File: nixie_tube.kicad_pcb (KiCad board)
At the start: 2 copper layers, 25.8 x 56.3 mm, 32 parts, among them J1 Conn_01x06_Male, J11 dc003a, J2 Conn_01x06_Female, J3 Conn_01x01_Male, J4 Conn_01x01_Female, Q1 SS8550, Q2 FQD5N60C, Q3 MMBTA42LT1, Q4 AO3407, U1 MC34063

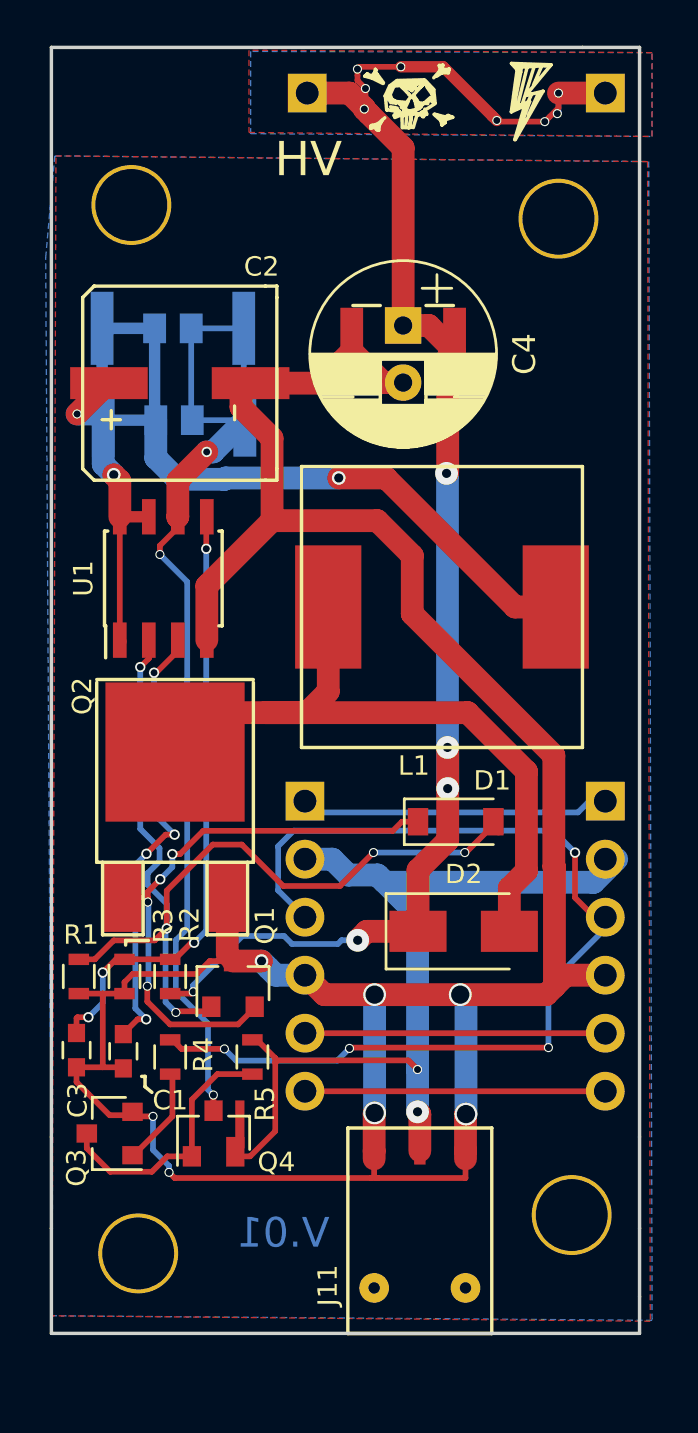
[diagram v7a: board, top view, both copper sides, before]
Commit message: added via stiching around the board
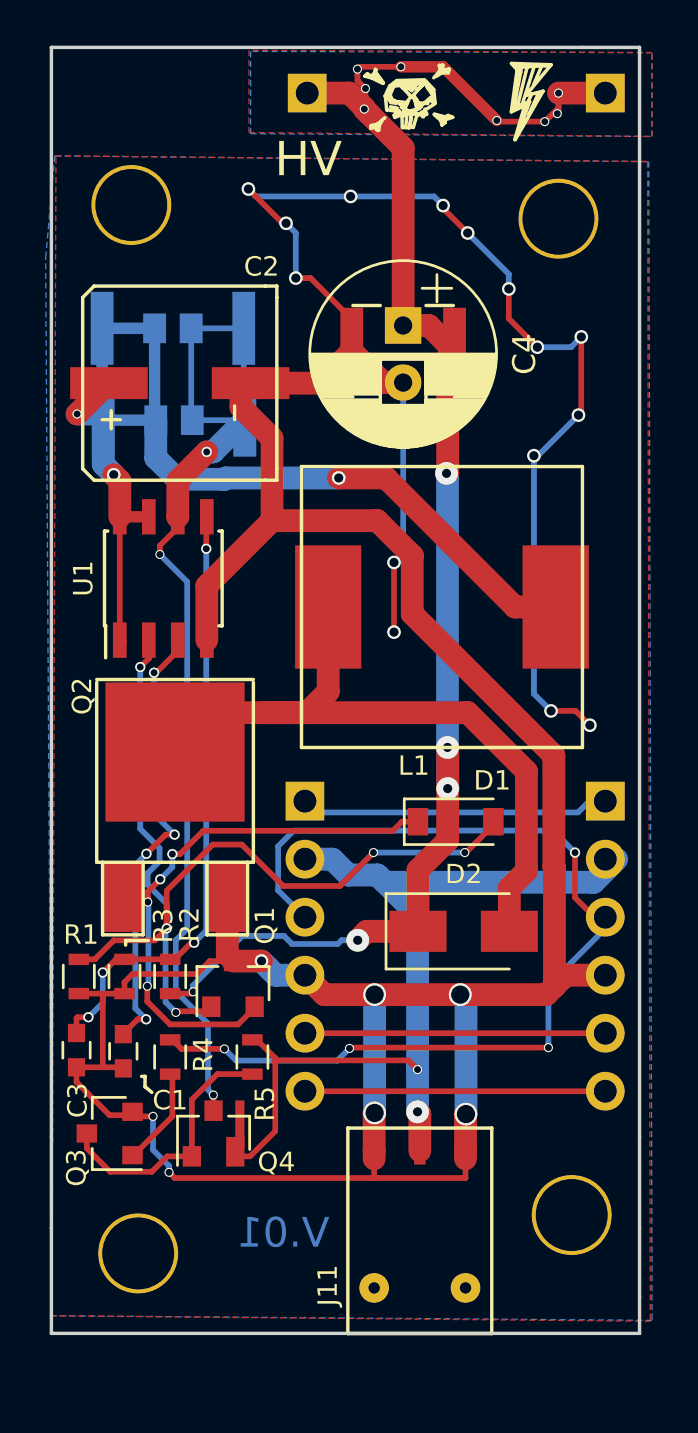
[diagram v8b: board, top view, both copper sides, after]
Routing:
- net GND: track 119.4 -> 178.4 mm, vias 7 -> 22
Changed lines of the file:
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@@
     (links 56)
     (no_connects 0)
-    (area 166.424999 79.724999 192.325001 136.175001)
+    (area 156.600001 76.825 202.925239 141.300001)
     (thickness 1.6)
     (drawings 27)
-    (tracks 374)
+    (tracks 419)
     (zones 0)
     (modules 32)
@@
   (segment (start 172.035 105.75) (end 172.035 106.225) (width 0.25) (layer F.Cu) (net 1) (status 30))
   (via (at 170.995547 107.175488) (size 0.453) (drill 0.3) (layers F.Cu B.Cu) (net 1))
+  (segment (start 188.375 108.85) (end 189.45 108.85) (width 0.25) (layer F.Cu) (net 2))
+  (via (at 190.075 109.475) (size 0.6) (drill 0.4) (layers F.Cu B.Cu) (net 2))
+  (segment (start 189.45 108.85) (end 190.075 109.475) (width 0.25) (layer F.Cu) (net 2))
+  (segment (start 187.625 97.675) (end 187.625 108.1) (width 0.25) (layer B.Cu) (net 2))
+  (segment (start 187.625 108.1) (end 188.375 108.85) (width 0.25) (layer B.Cu) (net 2))
+  (via (at 188.375 108.85) (size 0.6) (drill 0.4) (layers F.Cu B.Cu) (net 2))
+  (segment (start 188.498499 110.798501) (end 182.3 104.600002) (width 1) (layer F.Cu) (net 2))
+  (segment (start 181.5 102.35) (end 181.5 105.4) (width 0.25) (layer F.Cu) (net 2))
+  (via (at 181.5 105.4) (size 0.6) (drill 0.4) (layers F.Cu B.Cu) (net 2))
+  (segment (start 181.9 94.475) (end 181.9 101.95) (width 0.25) (layer B.Cu) (net 2))
+  (segment (start 181.9 101.95) (end 181.5 102.35) (width 0.25) (layer B.Cu) (net 2))
+  (via (at 181.5 102.35) (size 0.6) (drill 0.4) (layers F.Cu B.Cu) (net 2))
+  (segment (start 189.575 95.9) (end 187.8 97.675) (width 0.25) (layer B.Cu) (net 2))
+  (segment (start 187.8 97.675) (end 187.625 97.675) (width 0.25) (layer B.Cu) (net 2))
+  (via (at 187.625 97.675) (size 0.6) (drill 0.4) (layers F.Cu B.Cu) (net 2))
+  (segment (start 189.7 92.475) (end 189.7 95.775) (width 0.25) (layer F.Cu) (net 2))
+  (segment (start 189.7 95.775) (end 189.575 95.9) (width 0.25) (layer F.Cu) (net 2))
+  (via (at 189.575 95.9) (size 0.6) (drill 0.4) (layers F.Cu B.Cu) (net 2))
+  (segment (start 187.775 92.925) (end 189.25 92.925) (width 0.25) (layer B.Cu) (net 2))
+  (segment (start 189.25 92.925) (end 189.7 92.475) (width 0.25) (layer B.Cu) (net 2))
+  (via (at 189.7 92.475) (size 0.6) (drill 0.4) (layers F.Cu B.Cu) (net 2))
+  (segment (start 186.525 90.375) (end 186.525 91.675) (width 0.25) (layer F.Cu) (net 2))
+  (segment (start 186.525 91.675) (end 187.775 92.925) (width 0.25) (layer F.Cu) (net 2))
+  (via (at 187.775 92.925) (size 0.6) (drill 0.4) (layers F.Cu B.Cu) (net 2))
+  (segment (start 184.725 87.925) (end 186.525 89.725) (width 0.25) (layer B.Cu) (net 2))
+  (segment (start 186.525 89.725) (end 186.525 90.375) (width 0.25) (layer B.Cu) (net 2))
+  (via (at 186.525 90.375) (size 0.6) (drill 0.4) (layers F.Cu B.Cu) (net 2))
+  (segment (start 183.65 86.725) (end 183.65 86.85) (width 0.25) (layer F.Cu) (net 2))
+  (segment (start 183.65 86.85) (end 184.725 87.925) (width 0.25) (layer F.Cu) (net 2))
+  (via (at 184.725 87.925) (size 0.6) (drill 0.4) (layers F.Cu B.Cu) (net 2))
+  (segment (start 179.6 86.325) (end 183.25 86.325) (width 0.25) (layer B.Cu) (net 2))
+  (segment (start 183.25 86.325) (end 183.65 86.725) (width 0.25) (layer B.Cu) (net 2))
+  (via (at 183.65 86.725) (size 0.6) (drill 0.4) (layers F.Cu B.Cu) (net 2))
+  (segment (start 175.125 86) (end 175.45 86.325) (width 0.25) (layer B.Cu) (net 2))
+  (segment (start 175.45 86.325) (end 179.6 86.325) (width 0.25) (layer B.Cu) (net 2))
+  (via (at 179.6 86.325) (size 0.6) (drill 0.4) (layers F.Cu B.Cu) (net 2))
+  (segment (start 176.775 87.5) (end 176.625 87.5) (width 0.25) (layer F.Cu) (net 2))
+  (segment (start 176.625 87.5) (end 175.125 86) (width 0.25) (layer F.Cu) (net 2))
+  (via (at 175.125 86) (size 0.6) (drill 0.4) (layers F.Cu B.Cu) (net 2))
+  (segment (start 177.2 89.9) (end 177.2 87.925) (width 0.25) (layer B.Cu) (net 2))
+  (segment (start 177.2 87.925) (end 176.775 87.5) (width 0.25) (layer B.Cu) (net 2))
+  (via (at 176.775 87.5) (size 0.6) (drill 0.4) (layers F.Cu B.Cu) (net 2))
+  (segment (start 179.65 93.1) (end 179.65 91.7) (width 0.25) (layer F.Cu) (net 2))
+  (segment (start 179.65 91.7) (end 177.85 89.9) (width 0.25) (layer F.Cu) (net 2))
+  (segment (start 177.85 89.9) (end 177.2 89.9) (width 0.25) (layer F.Cu) (net 2))
+  (via (at 177.2 89.9) (size 0.6) (drill 0.4) (layers F.Cu B.Cu) (net 2))
   (segment (start 175.999999 120.099999) (end 175.7 119.8) (width 1) (layer B.Cu) (net 2))
   (segment (start 176.32 120.42) (end 175.999999 120.099999) (width 1) (layer B.Cu) (net 2))
@@
   (segment (start 188.523499 115.694721) (end 188.498499 115.669721) (width 1) (layer F.Cu) (net 2))
   (segment (start 188.498499 115.669721) (end 188.498499 110.798501) (width 1) (layer F.Cu) (net 2))
-  (segment (start 188.498499 110.798501) (end 182.3 104.600002) (width 1) (layer F.Cu) (net 2))
   (segment (start 180.77 100.52) (end 176.16 100.52) (width 1) (layer F.Cu) (net 2))
   (segment (start 182.3 104.600002) (end 182.3 102.05) (width 1) (layer F.Cu) (net 2))
